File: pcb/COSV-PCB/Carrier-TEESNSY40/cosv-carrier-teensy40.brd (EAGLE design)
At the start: 108 x 30.5 mm, 25 parts, among them X1 057-006-1, X3 22-23-2031, X4 22-23-2031, X5 22-23-2031, X6 22-23-2031, X7 22-23-2031

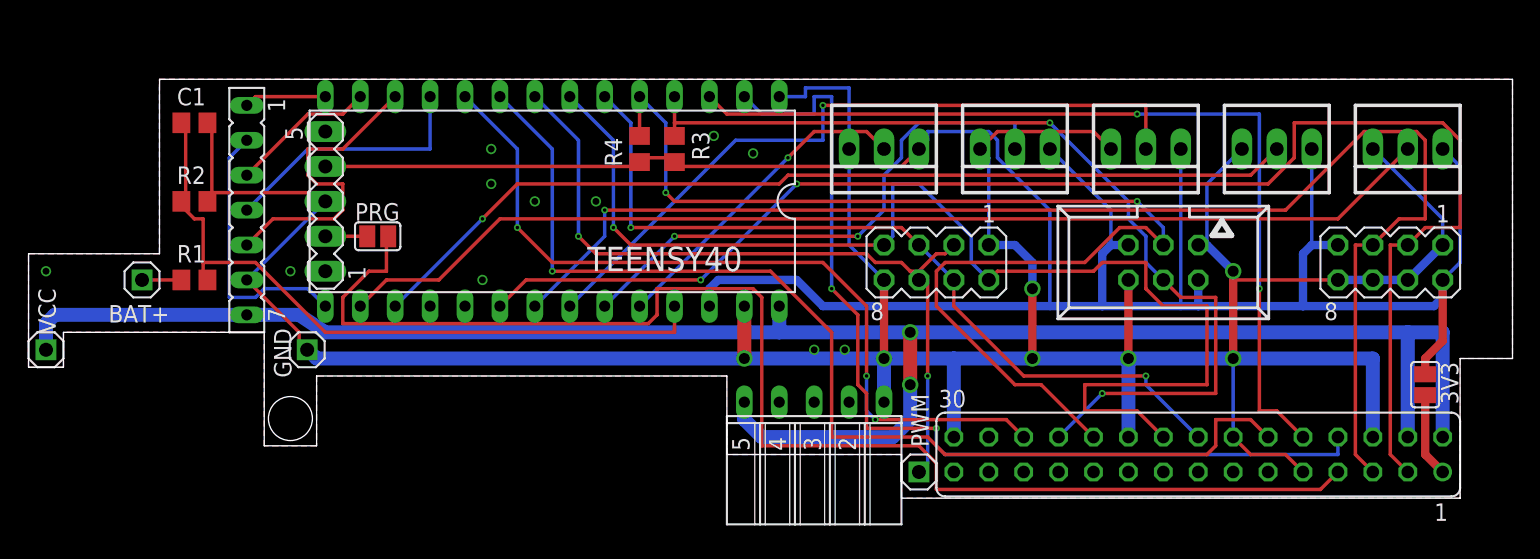
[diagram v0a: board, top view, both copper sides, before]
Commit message: Make the motor connector identical to the Arduino IBT_2 H-Bridge
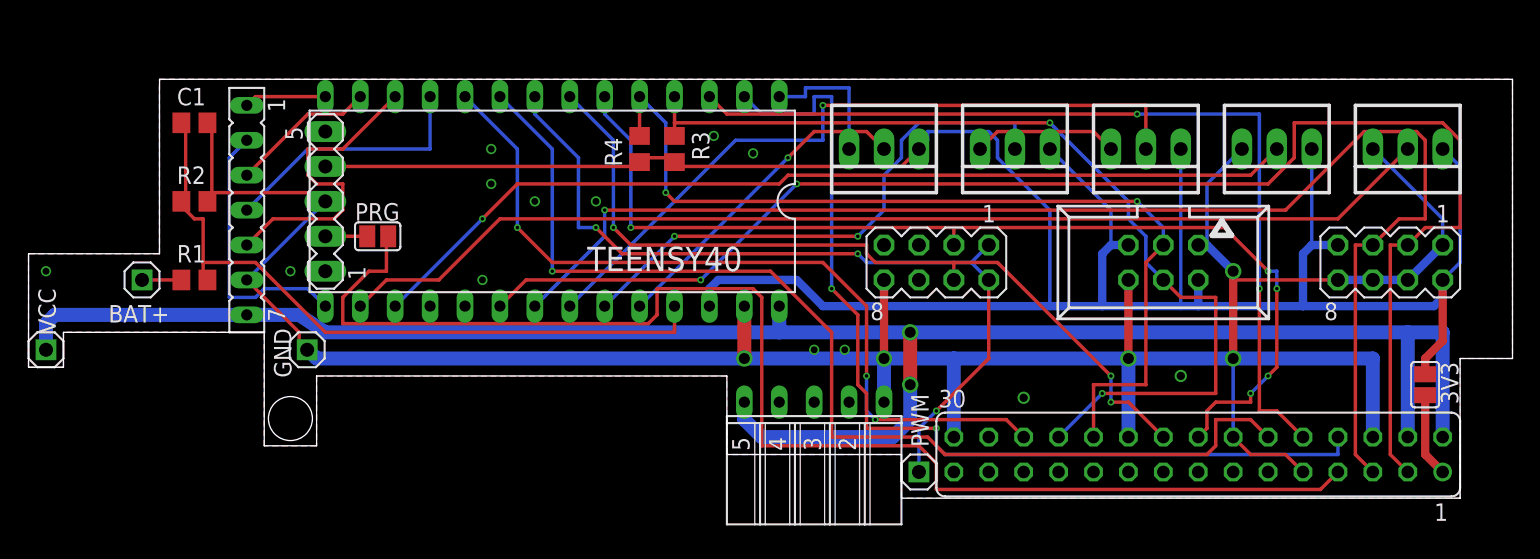
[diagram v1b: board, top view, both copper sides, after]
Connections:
- net N$2 renamed BAT+
- net GND: no longer SV3.1
- net L_EN: now also SV3.4; no longer SV3.2, SV3.7
- net PWM: now also SV3.1, SV3.2; no longer SV3.3, SV3.6
- net R_EN: now also SV3.3; no longer SV3.4, SV3.5
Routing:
- net L_EN: track 88.6 -> 59.9 mm, vias 1 -> 3
- net GND: track 248.4 -> 219.9 mm
- net ENCODER: track 85.4 -> 67.5 mm
- net R_EN: track 59.4 -> 75.8 mm, vias 2 -> 5
- net PWM: track 56.4 -> 60.1 mm, vias 2 -> 3

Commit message: Add second I2C channel to VISP connector
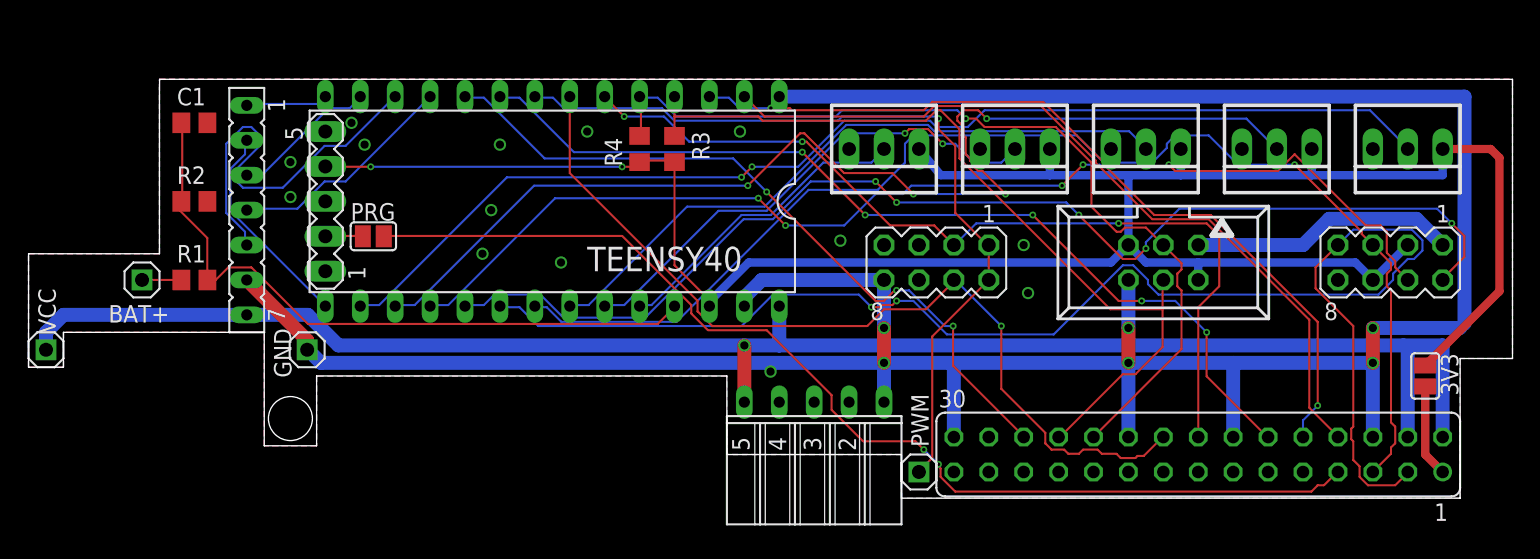
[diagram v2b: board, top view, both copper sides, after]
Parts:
- moved 3V3 0.64 mm to (100.3, 8.26)
- moved GOLD_ORB_SM1 0.45 mm to (27.0, 23.2)
- moved PRG 0.32 mm to (23.8, 18.4)
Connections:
- net 3V3: now also SV4.3, SV4.6; no longer SV4.2, SV4.7
- net GND: no longer SV4.4, SV4.6
- net SCL1: now also SV4.4
- net SDA0: now also SV4.7; no longer SV4.3
- net SDA1: now also SV4.2
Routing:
- net SDA1: track 0.00 -> 86.8 mm, vias 0 -> 5
- net SCL1: track 0.00 -> 82.8 mm, vias 0 -> 5
- net N$1: track 97.1 -> 79.1 mm, vias 0 -> 2
- net VCC: track 142.0 -> 124.8 mm, vias 2 -> 1
- net 3V3: track 182.4 -> 166.9 mm, vias 0 -> 2
- net A_PRESSURE: track 68.9 -> 83.3 mm, vias 1 -> 4
- net RX1: track 70.4 -> 58.0 mm, vias 2 -> 0
- net LINE_DETECT: track 79.0 -> 68.0 mm, vias 1 -> 5
- net R_EN: track 75.8 -> 65.5 mm, vias 5 -> 3
- net SCL0: track 100.0 -> 91.2 mm
- net GND: track 219.9 -> 227.8 mm, vias 18 -> 20
- net HOME: track 69.1 -> 61.3 mm, vias 2 -> 0
- net CS: track 22.6 -> 29.9 mm
- net TX1: track 66.1 -> 60.5 mm
- net PULSER: track 58.7 -> 53.4 mm
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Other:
- board text added: "VCC"
- board text added: "scl0"
- board text added: "scl1"
- board text added: "sda0"
- board text added: "sda1"
- board text removed: "SPI"
- board text removed: "scl"
- board text removed: "sda"

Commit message: Add Line Power Detect input and Watchdog Pulse output for alarm subsystem
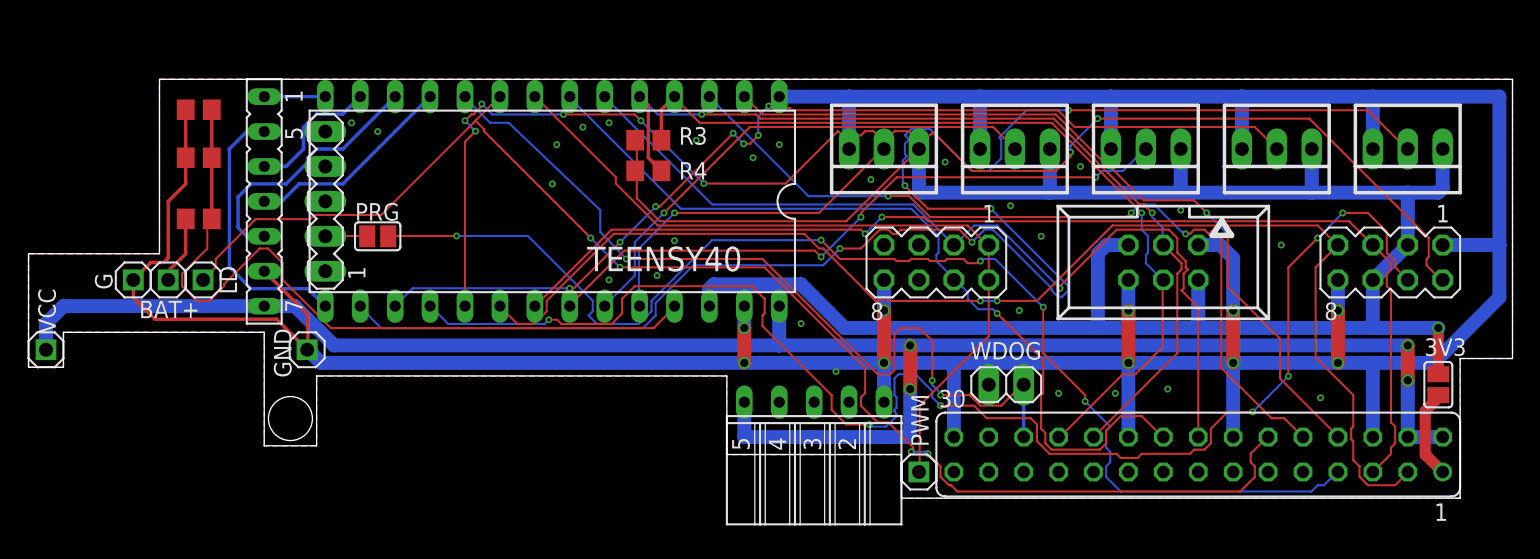
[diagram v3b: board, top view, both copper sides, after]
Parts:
- added G, LD: (no value), pinhead-2:1X01-S
- added WDOG: (no value), pinhead:1X02
- moved GOLD_ORB_SM1 5.08 mm to (32.1, 23.2)
- moved R1 4.46 mm to (11.1, 19.7)
- moved R2 3.19 mm to (11.1, 24.1), turned to 0 degrees
- moved R3 2.01 mm to (43.8, 25.4), turned to 180 degrees
- moved BAT+ 1.91 mm to (8.89, 15.2)
- moved R4 1.71 mm to (43.8, 23.2), turned to 180 degrees
- moved SV2 1.42 mm to (15.9, 21.0)
- moved 3V3 1.14 mm to (101.3, 7.62)
- moved C1 1.00 mm to (11.1, 27.6), turned to 180 degrees
- moved PRG 0.32 mm to (24.1, 18.4)
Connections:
- net 3V3: no longer SV1.4
- net GND: now also G.1, WDOG.1; no longer SV1.3
- net LINE_DETECT: now also LD.1
- net PULSER: now also WDOG.2
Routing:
- net GND: track 227.8 -> 275.5 mm, vias 20 -> 36
- net A_VOLUME: track 83.7 -> 120.7 mm, vias 2 -> 5
- net LINE_DETECT: track 68.0 -> 102.3 mm, vias 5 -> 4
- net SCL1: track 82.8 -> 102.8 mm, vias 5 -> 7
- net SDA1: track 86.8 -> 99.9 mm, vias 5 -> 8
- net SDA0: track 105.8 -> 93.0 mm
- net VCC: track 124.8 -> 135.8 mm, vias 1 -> 4
- net CS: track 29.9 -> 19.0 mm
- net A_PRESSURE: track 83.3 -> 72.9 mm, vias 4 -> 7
- net N$1: track 79.1 -> 89.5 mm, vias 2 -> 5
- net SCL0: track 91.2 -> 82.8 mm, vias 1 -> 2
- net PULSER: track 53.4 -> 61.6 mm
- net A_BATTERY: track 49.0 -> 55.5 mm
- net SCK: track 15.4 -> 19.8 mm
- net 3V3: track 166.9 -> 163.0 mm, vias 2 -> 1
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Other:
- board text removed: "VCC"

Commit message: New "millable" Carrier board for use with rPI3+ on COSV
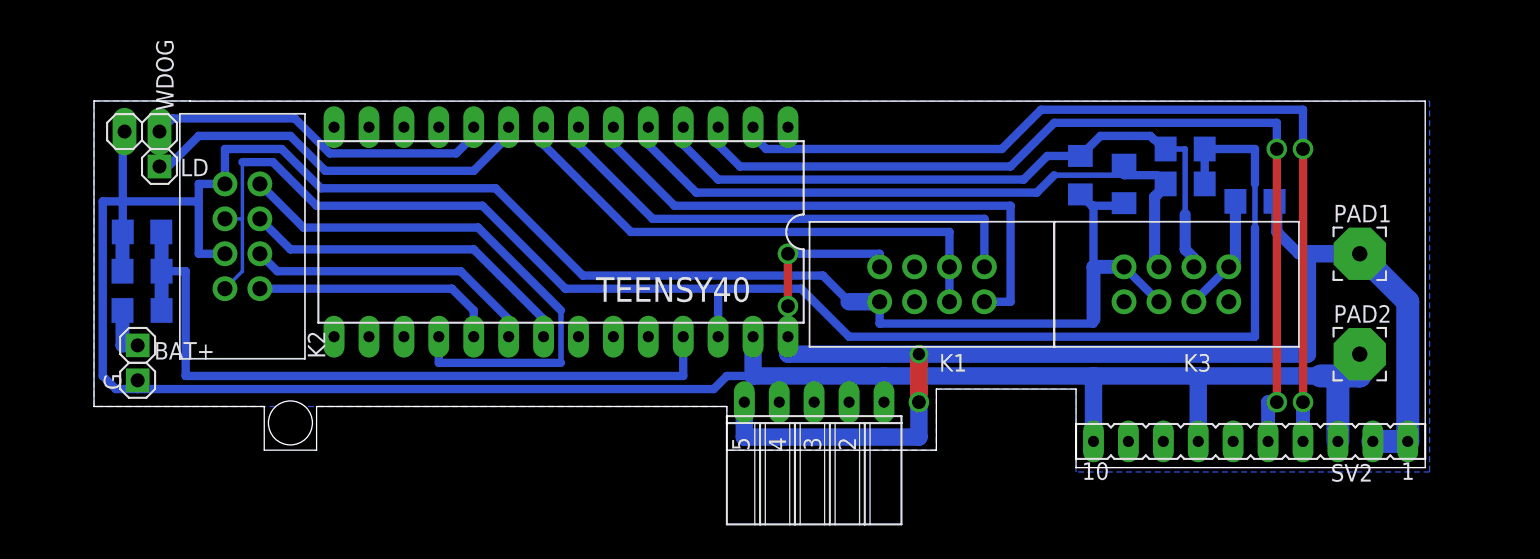
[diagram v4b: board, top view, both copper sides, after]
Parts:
- removed 3V3, PRG: (no value), jumper:SJ
- removed GND, PWM, VCC: (no value), pinhead-2:1X01-S
- removed SV1: (no value), con-lstb:MA05-1
- removed SV3, SV4: (no value), con-lstb:MA04-2
- removed SV8: (no value), con-lsta:FE15-2
- removed X1: 057-006-1, con-panduit:057-006-1
- removed X3, X4, X5, X6, X7: 22-23-2031, con-molex:22-23-2031
- added C2, C3: 10nf, rcl:C1206
- added K1, K2, K3: 61200821621, Wuerth_Elektronik_eiCan_05_Box_Header_IDC_Connectors_1_2:61200821621
- added PAD1, PAD2: WIREPAD3,81/1,1, wirepad:3,81/1,1
- added R5: 100, resistor:R1206
- C1: device rcl:C0805 -> rcl:C1206
- R1: device resistor:R0805 -> resistor:R1206
- R2: value 27k -> 22K; device resistor:R0805 -> resistor:R1206
- R3, R4: value 10K -> 2k2; device resistor:R0805 -> resistor:R1206
- SV2: device con-lsta:FE07 -> con-lsta:FE10
- moved SV2 73.8 mm to (87.6, 3.49), turned to 180 degrees
- moved WDOG 65.5 mm to (6.99, 26.0)
- moved R3 39.2 mm to (82.9, 22.2), flipped to the bottom
- moved R4 39.1 mm to (82.9, 24.8), flipped to the bottom
- moved C1 9.80 mm to (6.99, 18.7), flipped to the bottom, turned to 0 degrees
- moved R2 9.23 mm to (6.99, 15.9), flipped to the bottom, turned to 180 degrees
- moved LD 8.84 mm to (8.26, 23.5), turned to 0 degrees
- moved R1 7.84 mm to (6.99, 13.0), flipped to the bottom, turned to 180 degrees
- moved G 7.31 mm to (6.67, 7.94), turned to 0 degrees
- moved GOLD_ORB_SM1 6.30 mm to (27.3, 19.1), turned to 90 degrees
- moved BAT+ 5.26 mm to (6.67, 10.5), turned to 270 degrees
- moved TEENSY40 2.31 mm to (37.5, 18.7)
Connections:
- removed net A_MODE: TEENSY40.24, X3.2
- removed net A_PRESSURE: TEENSY40.17, X6.2
- removed net A_RATE: TEENSY40.23, X4.2
- removed net A_RATIO: TEENSY40.22, X5.2
- removed net A_VOLUME: TEENSY40.16, X7.2
- removed net CS: SV2.5, TEENSY40.12
- removed net DCRS: SV2.4, TEENSY40.11
- removed net MISO: SV2.1, TEENSY40.14
- removed net MOSI: SV2.3, TEENSY40.13
- removed net N$3: 3V3.2, SV8.1
- removed net ONOFF: SV1.1
- removed net PROGRAM: PRG.1, SV1.2
- removed net SCK: SV2.2, TEENSY40.15
- removed net VBAT: SV1.5
- net 3V3: now also K2.2, K2.6; no longer 3V3.1, SV4.3, SV4.6, X1.2, X1.5, X3.1, X4.1, X5.1, X6.1, X7.1
- net ENCODER: now also C3.1, K3.5, R3.1; no longer R4.1, SV8.22, X1.3
- net GND: now also C2.2, C3.2, K1.8, K2.4, K2.8, K3.6, K3.7, PAD2.1, SV2.10, SV2.3, SV2.7; no longer GND.1, SV2.6, SV3.8, SV4.1, SV4.8, SV8.14, SV8.20, SV8.30, SV8.6, SV8.9, TEENSY40.1, X1.1, X1.6, X3.3, X4.3, X5.3, X6.3, X7.3
- net HOME: now also C2.1, K3.3, R4.1; no longer R3.1, SV8.24, X1.4
- net LINE_DETECT: no longer SV8.12
- net L_EN: now also K1.1; no longer SV3.4, SV8.18
- net N$1: now also K3.1, K3.4, R5.1; no longer PRG.2, SV8.7
- net PULSER: no longer SV8.26
- net PWM: now also K1.3, K1.4; no longer PWM.1, SV3.1, SV3.2
- net RX1: now also SV2.4; no longer SV8.8
- net R_EN: now also K1.2; no longer SV3.3, SV8.16
- net SCL0: now also K2.5; no longer SV4.5, SV8.5
- net SCL1: now also K2.7; no longer SV4.4
- net SDA0: now also K2.3; no longer SV4.7, SV8.3
- net SDA1: now also K2.1; no longer SV4.2
- net TX1: now also SV2.5; no longer SV8.10
- net VCC: now also K1.7, PAD1.1, R5.2, SV2.1, SV2.2; no longer SV2.7, SV8.2, SV8.4, VCC.1
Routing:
- net A_VOLUME: track 120.7 -> 0.00 mm, vias 5 -> 0
- net SDA1: track 99.9 -> 18.1 mm, vias 8 -> 0
- net N$1: track 89.5 -> 8.55 mm, vias 5 -> 0
- net LINE_DETECT: track 102.3 -> 29.1 mm, vias 4 -> 0
- net A_PRESSURE: track 72.9 -> 0.00 mm, vias 7 -> 0
- net SDA0: track 93.0 -> 21.3 mm, vias 2 -> 0
- net SCL1: track 102.8 -> 40.3 mm, vias 7 -> 0
- net SCL0: track 82.8 -> 24.9 mm, vias 2 -> 0
- net 3V3: track 163.0 -> 113.3 mm, vias 1 -> 0
- net A_RATIO: track 47.4 -> 0.00 mm, vias 3 -> 0
- net A_RATE: track 37.3 -> 0.00 mm, vias 1 -> 0
- net PULSER: track 61.6 -> 25.5 mm, vias 3 -> 0
- net GND: track 275.5 -> 242.4 mm, vias 36 -> 0
- net VCC: track 135.8 -> 107.9 mm
- net R_EN: track 66.2 -> 40.9 mm, vias 1 -> 0
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- removed copper zone on layer 1, net GND
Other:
- board size 108 x 30.5 mm -> 96.8 x 26.7 mm
- board text removed: "CS"
- board text removed: "DC"
- board text removed: "miso"
- board text removed: "mode"
- board text removed: "mosi"
- board text removed: "pressure"
- board text removed: "rate"
- board text removed: "ratio"
- board text removed: "sck"
- board text removed: "volume"
